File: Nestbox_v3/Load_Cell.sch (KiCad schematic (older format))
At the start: 37 parts, among them J601 LOAD_CELL_CONN_01X04, Q601 DMG2301L-7 -- Replace by 0R, Q602 DMG3402L DNP, Q603 DMG2301L-7 DNP, Q604 DMG3402L DNP, U601 ADS1220

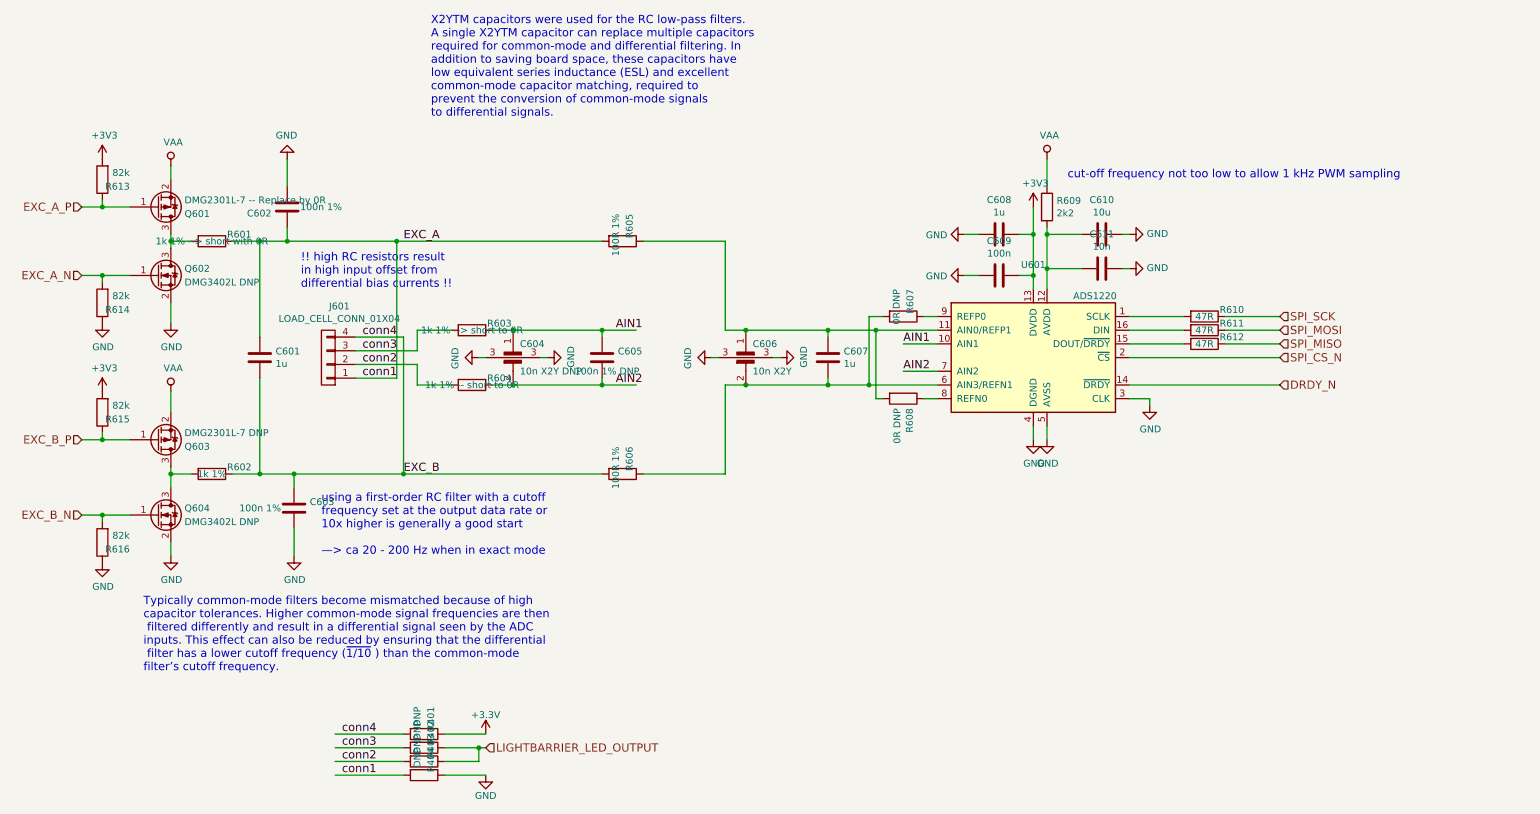
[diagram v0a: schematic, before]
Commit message: removed any unnecessary functions and connectors. corrected transistor bug
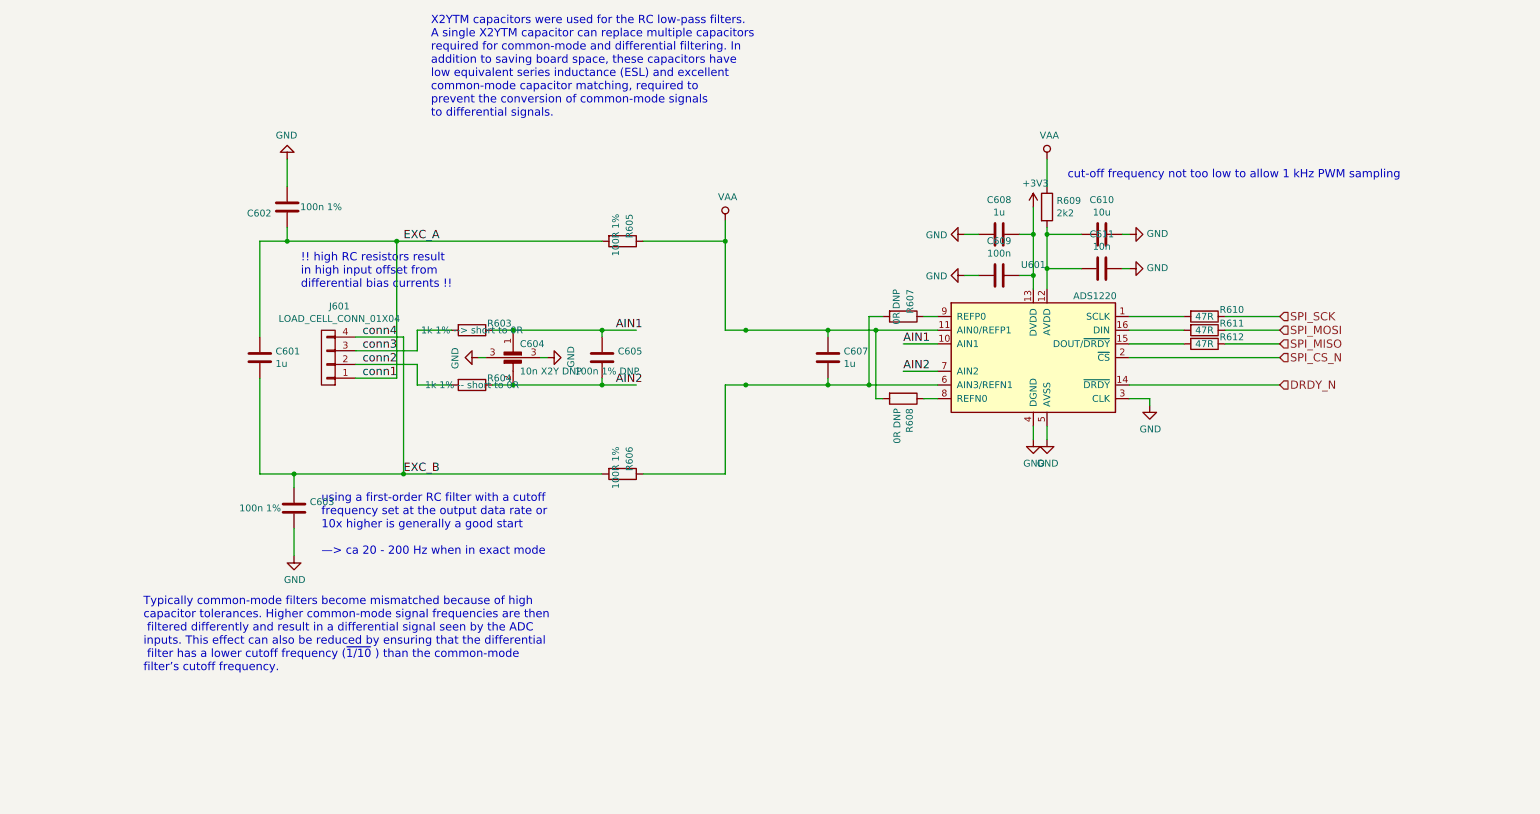
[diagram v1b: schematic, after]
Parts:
- removed C606: 10n X2Y, Octanis3:Capacitor_X2Y_603, symbol C_X2Y
- removed Q601: DMG2301L-7 -- Replace by 0R, TO_SOT_Packages_SMD:TSOT-23, symbol Q_PMOS_GSD
- removed Q602, Q604: DMG3402L DNP, TO_SOT_Packages_SMD:TSOT-23, symbol Q_NMOS_GSD
- removed Q603: DMG2301L-7 DNP, TO_SOT_Packages_SMD:TSOT-23, symbol Q_PMOS_GSD
- removed R401, R402, R403, R404: DNP, Resistors_SMD:R_0603, symbol R
- removed R601: 1k 1% --> short with 0R, Resistors_SMD:R_0603, symbol R
- removed R602: 1k 1%, Resistors_SMD:R_0603, symbol R
- removed R613, R614, R615, R616: 82k, Resistors_SMD:R_0603, symbol R
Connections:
- net labels removed: +3.3V, EXC_A_N, EXC_A_P, EXC_B_N, EXC_B_P, LIGHTBARRIER_LED_OUTPUT
- wire segments 90 -> 63

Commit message: finished V3 pcb. ORDERED
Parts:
- removed C604: 10n X2Y DNP, Octanis3:Capacitor_X2Y_603, symbol C_X2Y
- removed R609: 2k2, Resistors_SMD:R_0603, symbol R
- R607, R608: value 0R DNP -> DNP
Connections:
- net VAA: now also C610.2, C611.2, U601.12 (AVDD)
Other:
- note added: "performance "seems" better with 0R resistor here!"
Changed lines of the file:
@@
-$EndComp
-$Comp
-L R R609
-U 1 1 5AF73212
-P 8050 2900
-F 0 "R609" H 8120 2946 50  0000 L CNN
-F 1 "2k2" H 8120 2855 50  0000 L CNN
-F 2 "Resistors_SMD:R_0603" V 7980 2900 50  0001 C CNN
-F 3 "" H 8050 2900 50  0001 C CNN
-	1    8050 2900
-	1    0    0    -1
 $EndComp
 $Comp
@@
 $EndComp
 $Comp
-L GND #PWR057
-U 1 1 5AF756EC
-P 4400 4000
-F 0 "#PWR057" H 4400 3750 50  0001 C CNN
-F 1 "GND" H 4405 3827 50  0000 C CNN
-F 2 "" H 4400 4000 50  0001 C CNN
-F 3 "" H 4400 4000 50  0001 C CNN
-	1    4400 4000
-	0    -1   -1   0
-$EndComp
-$Comp
-L GND #PWR058
-U 1 1 5AF75761
-P 3900 4000
-F 0 "#PWR058" H 3900 3750 50  0001 C CNN
-F 1 "GND" H 3905 3827 50  0000 C CNN
-F 2 "" H 3900 4000 50  0001 C CNN
-F 3 "" H 3900 4000 50  0001 C CNN
-	1    3900 4000
-	0    1    1    0
-$EndComp
-$Comp
 L CONN_01X04 J601
 U 1 1 5AF75C36
@@
 $EndComp
 $Comp
-L GND #PWR059
+L GND #PWR057
 U 1 1 5AF76892
 P 8800 4350
-F 0 "#PWR059" H 8800 4100 50  0001 C CNN
+F 0 "#PWR057" H 8800 4100 50  0001 C CNN
 F 1 "GND" H 8805 4177 50  0000 C CNN
 F 2 "" H 8800 4350 50  0001 C CNN
@@
 EXC_B
 $Comp
-L VAA #PWR060
-U 1 1 5AF8BE8C
-P 5700 3000
-F 0 "#PWR060" H 5700 2850 50  0001 C CNN
-F 1 "VAA" H 5717 3173 50  0000 C CNN
-F 2 "" H 5700 3000 50  0001 C CNN
-F 3 "" H 5700 3000 50  0001 C CNN
-	1    5700 3000
-	1    0    0    -1
-$EndComp
-$Comp
-L VAA #PWR061
+L VAA #PWR058
 U 1 1 5AF8C129
-P 8050 2550
-F 0 "#PWR061" H 8050 2400 50  0001 C CNN
-F 1 "VAA" H 8067 2723 50  0000 C CNN
-F 2 "" H 8050 2550 50  0001 C CNN
-F 3 "" H 8050 2550 50  0001 C CNN
-	1    8050 2550
+P 8050 3050
+F 0 "#PWR058" H 8050 2900 50  0001 C CNN
+F 1 "VAA" H 8067 3223 50  0000 C CNN
+F 2 "" H 8050 3050 50  0001 C CNN
+F 3 "" H 8050 3050 50  0001 C CNN
+	1    8050 3050
 	1    0    0    -1
 $EndComp
@@
 P 7000 4300
 F 0 "R608" H 7070 4346 50  0000 L CNN
-F 1 "0R DNP" H 7070 4255 50  0000 L CNN
+F 1 "DNP" H 7070 4255 50  0000 L CNN
 F 2 "Resistors_SMD:R_0603" V 6930 4300 50  0001 C CNN
 F 3 "" H 7000 4300 50  0001 C CNN
@@
 P 7000 3700
 F 0 "R607" H 6800 3750 50  0000 L CNN
-F 1 "0R DNP" H 6800 3650 50  0000 L CNN
+F 1 "DNP" H 6800 3650 50  0000 L CNN
 F 2 "Resistors_SMD:R_0603" V 6930 3700 50  0001 C CNN
 F 3 "" H 7000 3700 50  0001 C CNN
 	1    7000 3700
 	0    1    1    0
-$EndComp
-$Comp
-L C_X2Y C604
-U 1 1 5AF92C07
-P 4150 4100
-F 0 "C604" H 4200 4300 50  0000 L CNN
-F 1 "10n X2Y DNP" H 4200 4100 50  0000 L CNN
-F 2 "Octanis3:Capacitor_X2Y_603" V 4150 4100 50  0001 C CNN
-F 3 "" V 4150 4100 50  0001 C CNN
-	1    4150 4100
-	1    0    0    -1
 $EndComp
 $Comp
@@
 Wire Wire Line
 	2300 3150 4800 3150
-Wire Wire Line
-	8050 2550 8050 2750
 Connection ~ 3300 3150
 Wire Wire Line
@@
 Wire Wire Line
 	7150 3700 7250 3700
-Wire Wire Line
-	4400 4000 4350 4000
-Wire Wire Line
-	3900 4000 3950 4000
 Connection ~ 4800 3800
 Connection ~ 4150 3800
@@
 	5100 3150 5700 3150
 Wire Wire Line
-	5700 3000 5700 3800
-Connection ~ 5850 3800
-Wire Wire Line
 	5700 4200 5700 4850
 Wire Wire Line
 	5700 4850 5100 4850
-Connection ~ 5850 4200
 Text HLabel 9750 3700 2    60   Input ~ 0
 SPI_SCK
@@
 Wire Wire Line
 	2300 4850 4800 4850
-Connection ~ 5700 3150
 $Comp
 L R R605
@@
 	2550 4850 2550 4950
 $Comp
-L GND #PWR062
+L GND #PWR059
 U 1 1 5AF8D573
 P 2550 5450
-F 0 "#PWR062" H 2550 5200 50  0001 C CNN
+F 0 "#PWR059" H 2550 5200 50  0001 C CNN
 F 1 "GND" H 2555 5277 50  0000 C CNN
 F 2 "" H 2550 5450 50  0001 C CNN
@@
 	2500 2550 2500 2750
 $Comp
-L GND #PWR063
+L GND #PWR060
 U 1 1 5AF8D7AF
 P 2500 2550
-F 0 "#PWR063" H 2500 2300 50  0001 C CNN
+F 0 "#PWR060" H 2500 2300 50  0001 C CNN
 F 1 "GND" H 2505 2377 50  0000 C CNN
 F 2 "" H 2500 2550 50  0001 C CNN
@@
 $EndComp
 Wire Wire Line
+	5700 3150 5700 3800
+Wire Wire Line
+	5950 3650 5950 3800
+Connection ~ 5950 3800
+Wire Wire Line
 	2300 3150 2300 3850
+$Comp
+L VAA #PWR061
+U 1 1 5BCCBEFB
+P 5950 3650
+F 0 "#PWR061" H 5950 3500 50  0001 C CNN
+F 1 "VAA" H 5967 3823 50  0000 C CNN
+F 2 "" H 5950 3650 50  0001 C CNN
+F 3 "" H 5950 3650 50  0001 C CNN
+	1    5950 3650
+	1    0    0    -1
+$EndComp
+Text Notes 4300 2850 0    60   ~ 0
+performance "seems" better with 0R resistor here!
 $EndSCHEMATC

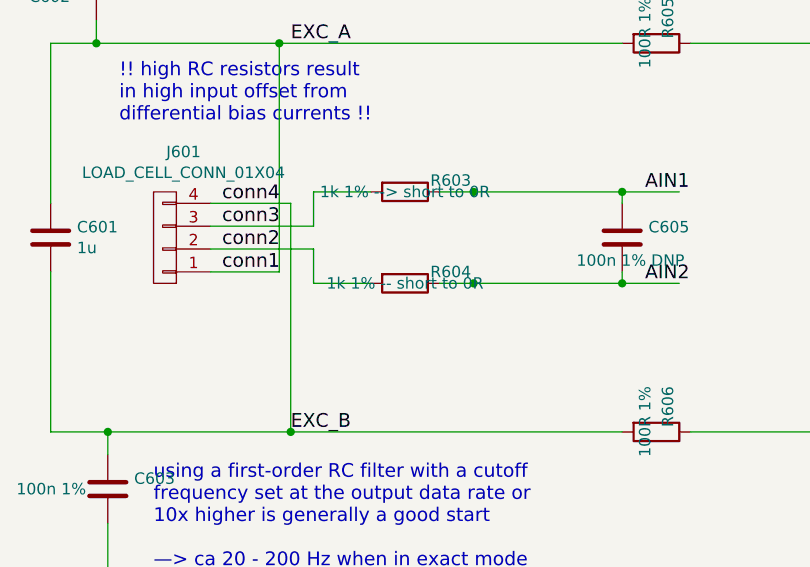
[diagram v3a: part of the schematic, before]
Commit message: exchanged both inductor footprints.
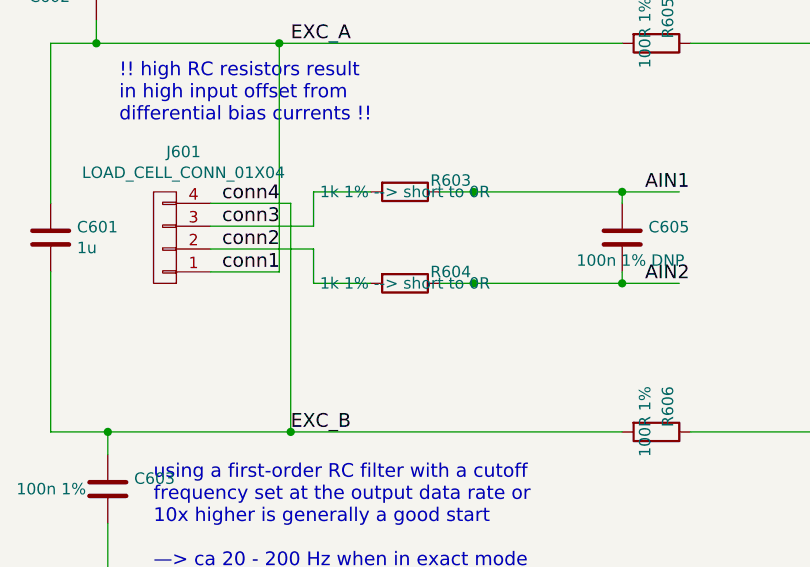
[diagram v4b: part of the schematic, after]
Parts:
- R604: value 1k 1% -- short to 0R -> 1k 1% --> short to 0R
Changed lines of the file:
@@
 P 3850 4200
 F 0 "R604" V 3800 4400 50  0000 C CNN
-F 1 "1k 1% -- short to 0R" V 3850 4200 50  0000 C CNN
+F 1 "1k 1% --> short to 0R" V 3850 4200 50  0000 C CNN
 F 2 "Resistors_SMD:R_0603" V 3780 4200 50  0001 C CNN
 F 3 "" H 3850 4200 50  0001 C CNN

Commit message: added MPN for all components for PCBA
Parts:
- C601, C607, C608: MPN (none) -> CC0603KRX7R8BB105
- C602, C603: MPN (none) -> CC0603JRX7R7BB104
- C609: MPN (none) -> CC0603KRX7R9BB104
- C610: MPN (none) -> CC0805KKX5R8BB106
- R605, R606: MPN (none) -> RC0603FR-07100RL
- R610, R611, R612: MPN (none) -> RC0603JR-0747RL; SKU (none) -> 301010091
- U601: MPN (none) -> ADS1220IPW
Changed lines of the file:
@@
-EESchema Schematic File Version 2
+EESchema Schematic File Version 4
 LIBS:power
 LIBS:device
@@
 LIBS:contrib
 LIBS:valves
-LIBS:Octanis3
 LIBS:Nestbox_v2-cache
-EELAYER 25 0
+EELAYER 26 0
 EELAYER END
 $Descr A4 11693 8268
@@
 F 2 "Capacitors_SMD:C_0805" H 8488 2950 50  0001 C CNN
 F 3 "" H 8450 3100 50  0001 C CNN
+F 4 "CC0805KKX5R8BB106" H 0   0   50  0001 C CNN "MPN"
 	1    8450 3100
 	0    1    1    0
@@
 F 2 "Capacitors_SMD:C_0603" H 7738 3250 50  0001 C CNN
 F 3 "" H 7700 3400 50  0001 C CNN
+F 4 "CC0603KRX7R9BB104" H 0   0   50  0001 C CNN "MPN"
 	1    7700 3400
 	0    -1   -1   0
@@
 F 2 "Capacitors_SMD:C_0603" H 7738 2950 50  0001 C CNN
 F 3 "" H 7700 3100 50  0001 C CNN
+F 4 "CC0603KRX7R8BB105" H 0   0   50  0001 C CNN "MPN"
 	1    7700 3100
 	0    1    1    0
@@
 F 2 "Capacitors_SMD:C_0603" H 6488 3850 50  0001 C CNN
 F 3 "" H 6450 4000 50  0001 C CNN
+F 4 "CC0603KRX7R8BB105" H 0   0   50  0001 C CNN "MPN"
 	1    6450 4000
 	1    0    0    -1
@@
 F 2 "Resistors_SMD:R_0603" V 9130 3900 50  0001 C CNN
 F 3 "" H 9200 3900 50  0001 C CNN
+F 4 "RC0603JR-0747RL" H 0   0   50  0001 C CNN "MPN"
+F 5 "301010091" H 0   0   50  0001 C CNN "SKU"
 	1    9200 3900
 	0    1    1    0
@@
 F 2 "Resistors_SMD:R_0603" V 9130 3800 50  0001 C CNN
 F 3 "" H 9200 3800 50  0001 C CNN
+F 4 "RC0603JR-0747RL" H 0   0   50  0001 C CNN "MPN"
+F 5 "301010091" H 0   0   50  0001 C CNN "SKU"
 	1    9200 3800
 	0    1    1    0
@@
 F 2 "Resistors_SMD:R_0603" V 9130 3700 50  0001 C CNN
 F 3 "" H 9200 3700 50  0001 C CNN
+F 4 "RC0603JR-0747RL" H 0   0   50  0001 C CNN "MPN"
+F 5 "301010091" H 0   0   50  0001 C CNN "SKU"
 	1    9200 3700
 	0    1    1    0
@@
 F 2 "Housings_SSOP:TSSOP-16_4.4x5mm_Pitch0.65mm" H 8200 4550 50  0001 L CNN
 F 3 "" H 7450 4400 50  0001 C CNN
+F 4 "ADS1220IPW" H 0   0   50  0001 C CNN "MPN"
 	1    7950 4000
 	1    0    0    -1
@@
 F 2 "Resistors_SMD:R_0603" V 4880 4850 50  0001 C CNN
 F 3 "" H 4950 4850 50  0001 C CNN
+F 4 "RC0603FR-07100RL" H 0   0   50  0001 C CNN "MPN"
 	1    4950 4850
 	0    1    1    0
@@
 F 2 "Resistors_SMD:R_0603" V 4880 3150 50  0001 C CNN
 F 3 "" H 4950 3150 50  0001 C CNN
+F 4 "RC0603FR-07100RL" H 0   0   50  0001 C CNN "MPN"
 	1    4950 3150
 	0    1    1    0
@@
 F 2 "Capacitors_SMD:C_0603" H 2338 3850 50  0001 C CNN
 F 3 "" H 2300 4000 50  0001 C CNN
+F 4 "CC0603KRX7R8BB105" H 0   0   50  0001 C CNN "MPN"
 	1    2300 4000
 	1    0    0    -1
@@
 F 2 "Capacitors_SMD:C_0603" H 2588 4950 50  0001 C CNN
 F 3 "" H 2550 5100 50  0001 C CNN
+F 4 "CC0603JRX7R7BB104" H 0   0   50  0001 C CNN "MPN"
 	1    2550 5100
 	1    0    0    -1
@@
 F 2 "Capacitors_SMD:C_0603" H 2538 2750 50  0001 C CNN
 F 3 "" H 2500 2900 50  0001 C CNN
+F 4 "CC0603JRX7R7BB104" H 0   0   50  0001 C CNN "MPN"
 	1    2500 2900
 	-1   0    0    1

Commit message: reworked silk layer for PCBA. generated position files. reviewed parts MPN for final order
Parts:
- C611: MPN (none) -> CC0603KRX7R9BB103
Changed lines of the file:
@@
-EESchema Schematic File Version 4
+EESchema Schematic File Version 2
 LIBS:power
 LIBS:device
@@
 LIBS:contrib
 LIBS:valves
+LIBS:Octanis3
 LIBS:Nestbox_v2-cache
-EELAYER 26 0
+EELAYER 25 0
 EELAYER END
 $Descr A4 11693 8268
@@
 F 2 "Capacitors_SMD:C_0603" H 8488 3200 50  0001 C CNN
 F 3 "" H 8450 3350 50  0001 C CNN
+F 4 "CC0603KRX7R9BB103" V 8450 3350 60  0001 C CNN "MPN"
 	1    8450 3350
 	0    1    1    0
